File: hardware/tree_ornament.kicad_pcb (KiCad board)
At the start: 2 copper layers, 21 parts, among them J1 Conn_02x03_Counter_Clockwise, SW1 TL1107BF130WQ, U1 ATtiny85-20P

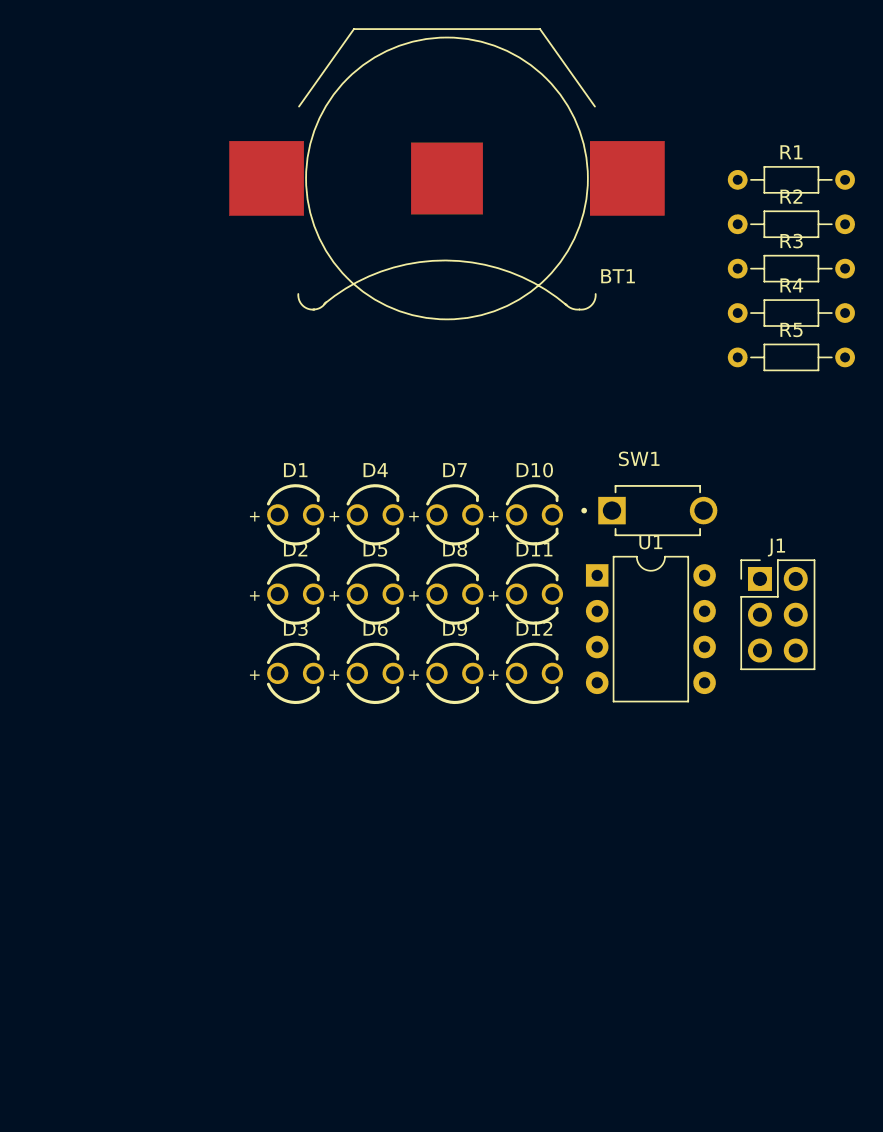
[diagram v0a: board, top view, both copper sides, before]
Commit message: Added silkscreen/edge cuts, placed footprints, initial release
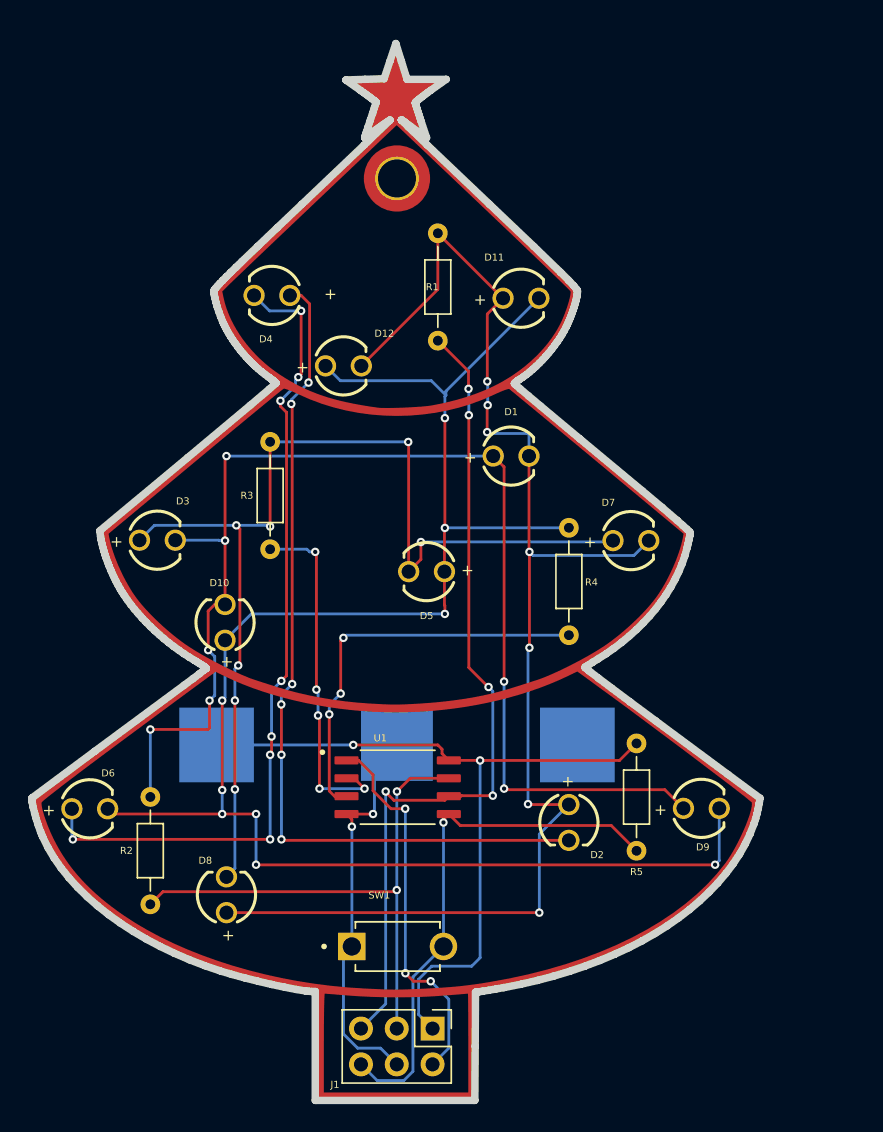
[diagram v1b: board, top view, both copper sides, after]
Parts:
- added G***: LOGO, tree_ornament:oshw_logo, B.Cu at (145.3, 75.6)
- added G***: LOGO, tree_ornament:lamemakes_logo, B.Cu at (139.9, 75.1)
- added REF**: MountingHole_2.7mm_M2.5_DIN965_Pad_TopOnly, MountingHole:MountingHole_2.7mm_M2.5_DIN965_Pad_TopOnly, F.Cu at (141.6, 67.9)
- added REF**: tree_outline, tree_ornament:tree_outline, F.Cu at (141.6, 95.8)
- BT1: moved to B.Cu
- U1: footprint Package_DIP:DIP-8_W7.62mm -> tree_ornament:SOIC127P798X216-8N
- moved R2 58.2 mm to (124.1, 111.8), turned to -90 degrees
- moved BT1 40.4 mm to (141.6, 108.1), turned to 0 degrees
- moved J1 39.5 mm to (144.1, 128.2), turned to -90 degrees
- moved SW1 36.0 mm to (141.7, 122.4)
- moved R3 35.4 mm to (132.6, 86.6), turned to -90 degrees
- moved R5 28.3 mm to (158.6, 108.0), turned to -90 degrees
- moved D8 26.8 mm to (129.5, 118.7), turned to 90 degrees
- moved D12 25.7 mm to (137.8, 81.2)
- moved D2 25.3 mm to (153.8, 113.6), turned to -90 degrees
- moved D10 23.2 mm to (129.4, 99.4), turned to 90 degrees
- moved D6 22.4 mm to (119.8, 112.6)
- moved R1 21.6 mm to (144.5, 71.8), turned to -90 degrees
- moved D11 21.0 mm to (150.4, 76.4)
- moved U1 20.6 mm to (141.7, 111.1)
- moved D9 19.9 mm to (163.2, 112.6)
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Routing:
- net Net-(D10-K): track 0.00 -> 123.2 mm, vias 0 -> 9
- net Net-(D1-A): track 0.00 -> 100.2 mm, vias 0 -> 7
- net Net-(D1-K): track 0.00 -> 89.3 mm, vias 0 -> 7
- net Net-(D3-K): track 0.00 -> 76.3 mm, vias 0 -> 7
- net Net-(D2-A): track 0.00 -> 61.1 mm, vias 0 -> 6
- net /MISO: track 0.00 -> 59.5 mm, vias 0 -> 5
- net Net-(D4-A): track 0.00 -> 58.8 mm, vias 0 -> 8
- net /+3v: track 0.00 -> 53.8 mm, vias 0 -> 2
- net /SCK: track 0.00 -> 38.8 mm, vias 0 -> 2
- net /MOSI: track 0.00 -> 38.1 mm, vias 0 -> 1
- net Net-(U1-XTAL2/PB4): track 0.00 -> 28.7 mm, vias 0 -> 3
- net GND: track 0.00 -> 28.2 mm, vias 0 -> 2
- net /RST: track 0.00 -> 26.9 mm, vias 0 -> 3
- net Net-(U1-XTAL1/PB3): track 0.00 -> 25.0 mm, vias 0 -> 5
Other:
- board outline added: 51.7 x 75 mm
- board text added: "2024 v0.1"

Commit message: Found unconnected LEDs, cleaned up firmware code
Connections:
- D2 pad 2: Net-(D2-A) -> Net-(D1-K)
- D4 pad 1: Net-(D2-A) -> Net-(D1-K)
- D4 pad 2: Net-(D4-A) -> Net-(D3-K)
- D6 pad 1: Net-(D4-A) -> Net-(D3-K)
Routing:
- net Net-(D1-K): track 89.3 -> 156.2 mm, vias 7 -> 13
- net Net-(D2-A): track 61.1 -> 0.00 mm, vias 6 -> 0
- net Net-(D3-K): track 76.3 -> 136.5 mm, vias 7 -> 15
- net Net-(D4-A): track 58.8 -> 0.00 mm, vias 8 -> 0
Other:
- board text added: "2024 v0.2"
- board text removed: "2024 v0.1"

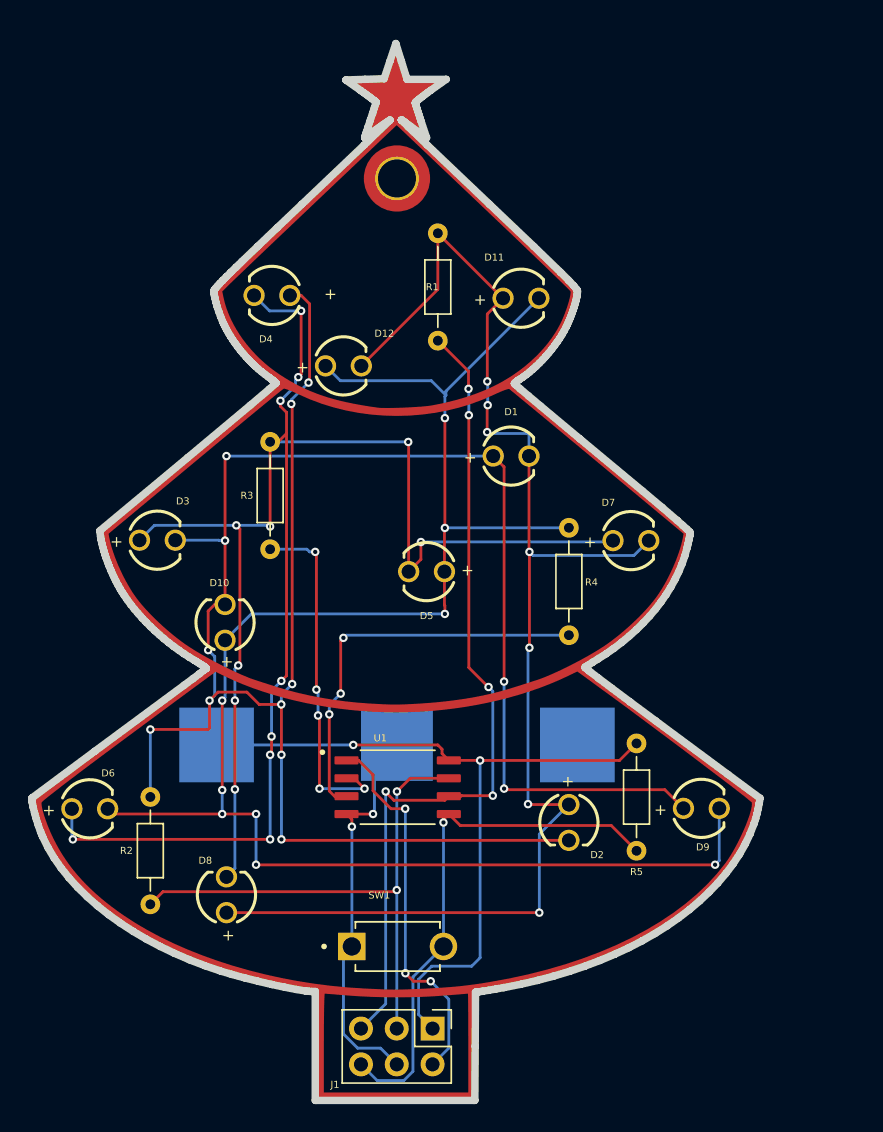
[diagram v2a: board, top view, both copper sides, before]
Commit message: Fixed swapped pins
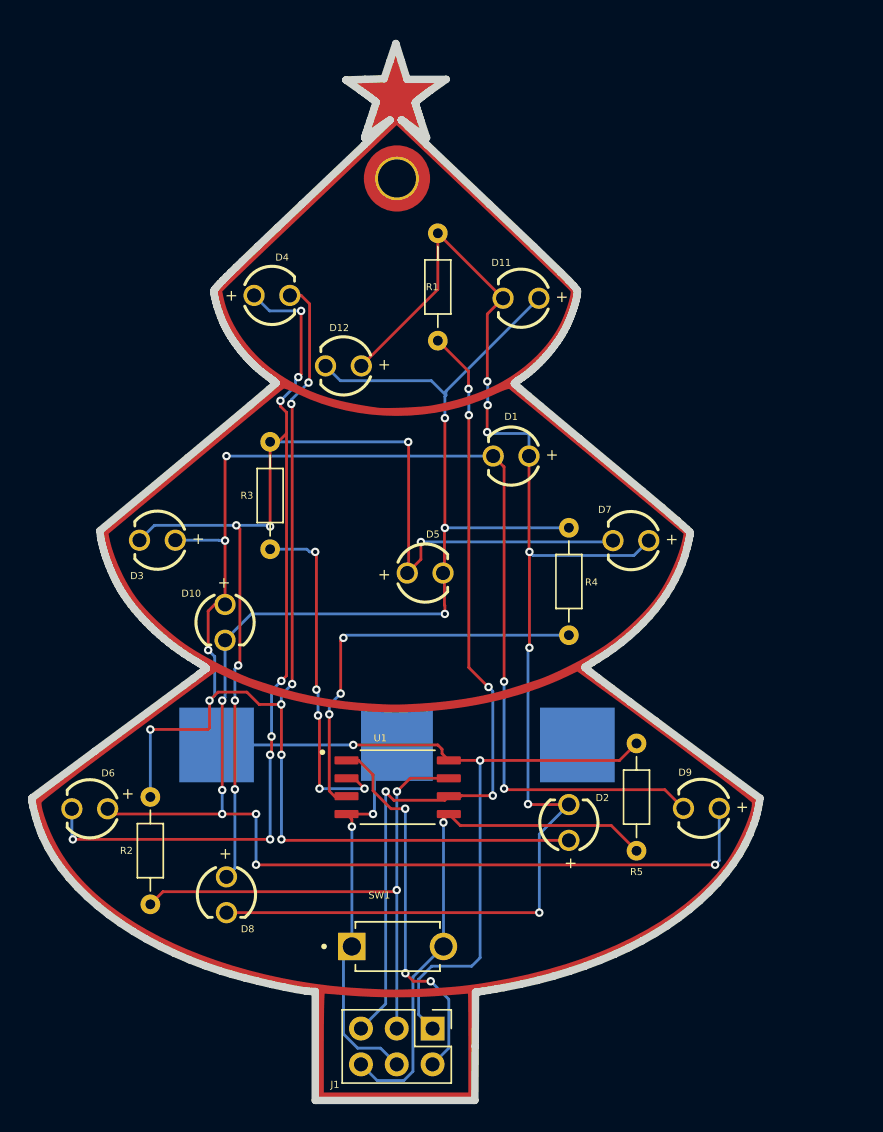
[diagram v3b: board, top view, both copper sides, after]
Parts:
- moved D5 0.14 mm to (143.6, 95.9), turned to 0 degrees
- turned D1 to 180 degrees
- turned D10 to -90 degrees
- turned D11 to 180 degrees
- turned D12 to 180 degrees
- turned D2 to 90 degrees
- turned D3 to 180 degrees
- turned D4 to 0 degrees
- turned D6 to 180 degrees
- turned D7 to 180 degrees
- turned D8 to -90 degrees
- turned D9 to 180 degrees
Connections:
- D1 pad 1: Net-(D1-K) -> Net-(D1-A)
- D1 pad 2: Net-(D1-A) -> Net-(D1-K)
- D10 pad 1: Net-(D10-K) -> Net-(D1-K)
- D10 pad 2: Net-(D1-K) -> Net-(D10-K)
- D11 pad 1: Net-(D1-A) -> Net-(D10-K)
- D11 pad 2: Net-(D10-K) -> Net-(D1-A)
- D12 pad 1: Net-(D10-K) -> Net-(D1-A)
- D12 pad 2: Net-(D1-A) -> Net-(D10-K)
- D2 pad 1: Net-(D1-A) -> Net-(D1-K)
- D2 pad 2: Net-(D1-K) -> Net-(D1-A)
- D3 pad 1: Net-(D3-K) -> Net-(D1-K)
- D3 pad 2: Net-(D1-K) -> Net-(D3-K)
- D4 pad 1: Net-(D1-K) -> Net-(D3-K)
- D4 pad 2: Net-(D3-K) -> Net-(D1-K)
- D5 pad 1: Net-(D10-K) -> Net-(D3-K)
- D5 pad 2: Net-(D3-K) -> Net-(D10-K)
- D6 pad 1: Net-(D3-K) -> Net-(D10-K)
- D6 pad 2: Net-(D10-K) -> Net-(D3-K)
- D7 pad 1: Net-(D3-K) -> Net-(D1-A)
- D7 pad 2: Net-(D1-A) -> Net-(D3-K)
- D8 pad 1: Net-(D1-A) -> Net-(D3-K)
- D8 pad 2: Net-(D3-K) -> Net-(D1-A)
- D9 pad 1: Net-(D1-K) -> Net-(D10-K)
- D9 pad 2: Net-(D10-K) -> Net-(D1-K)
